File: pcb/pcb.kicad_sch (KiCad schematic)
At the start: 4 parts, among them U1 ESP32-WROOM-32, U2 SCD41-D-R2, U3 BME680, U4 HD44780_I2C

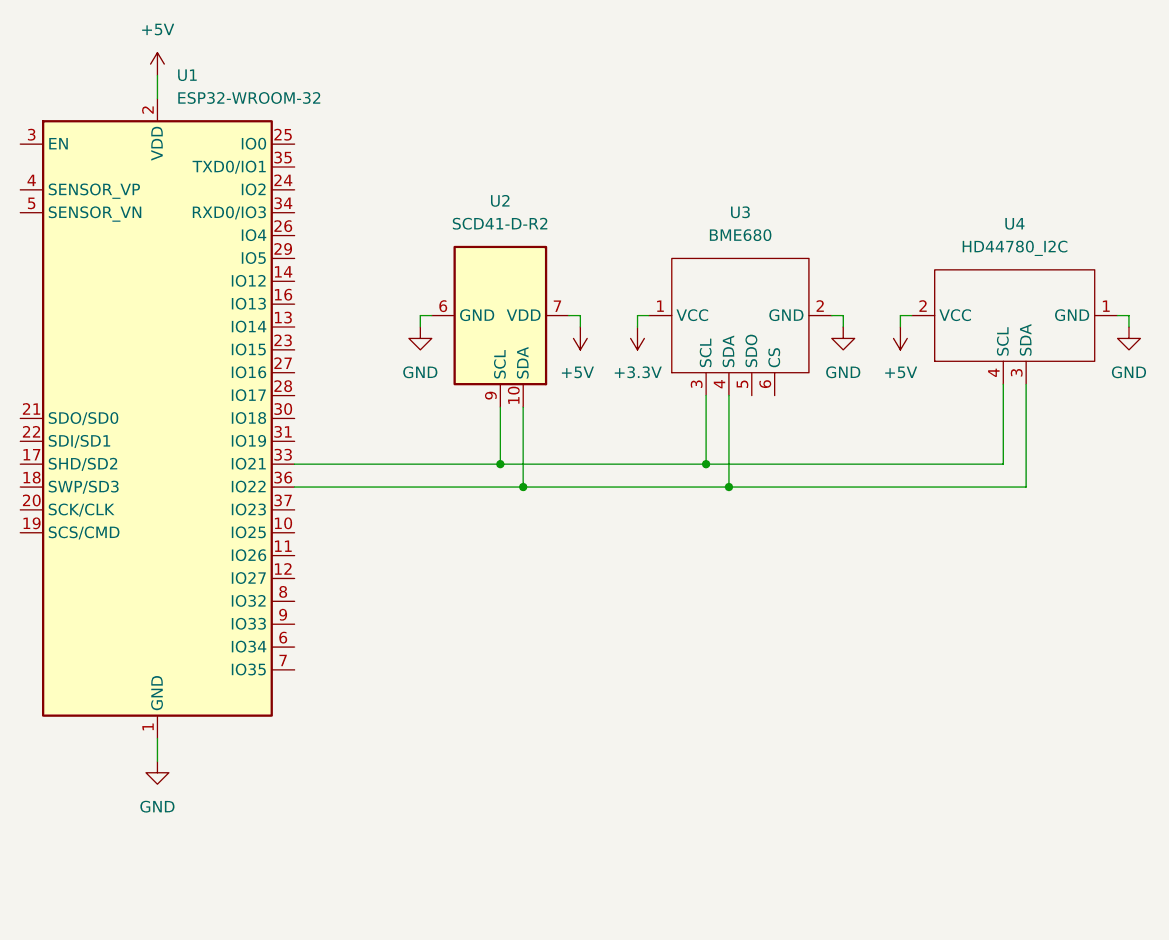
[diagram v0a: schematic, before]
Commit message: add pullup resistors to design
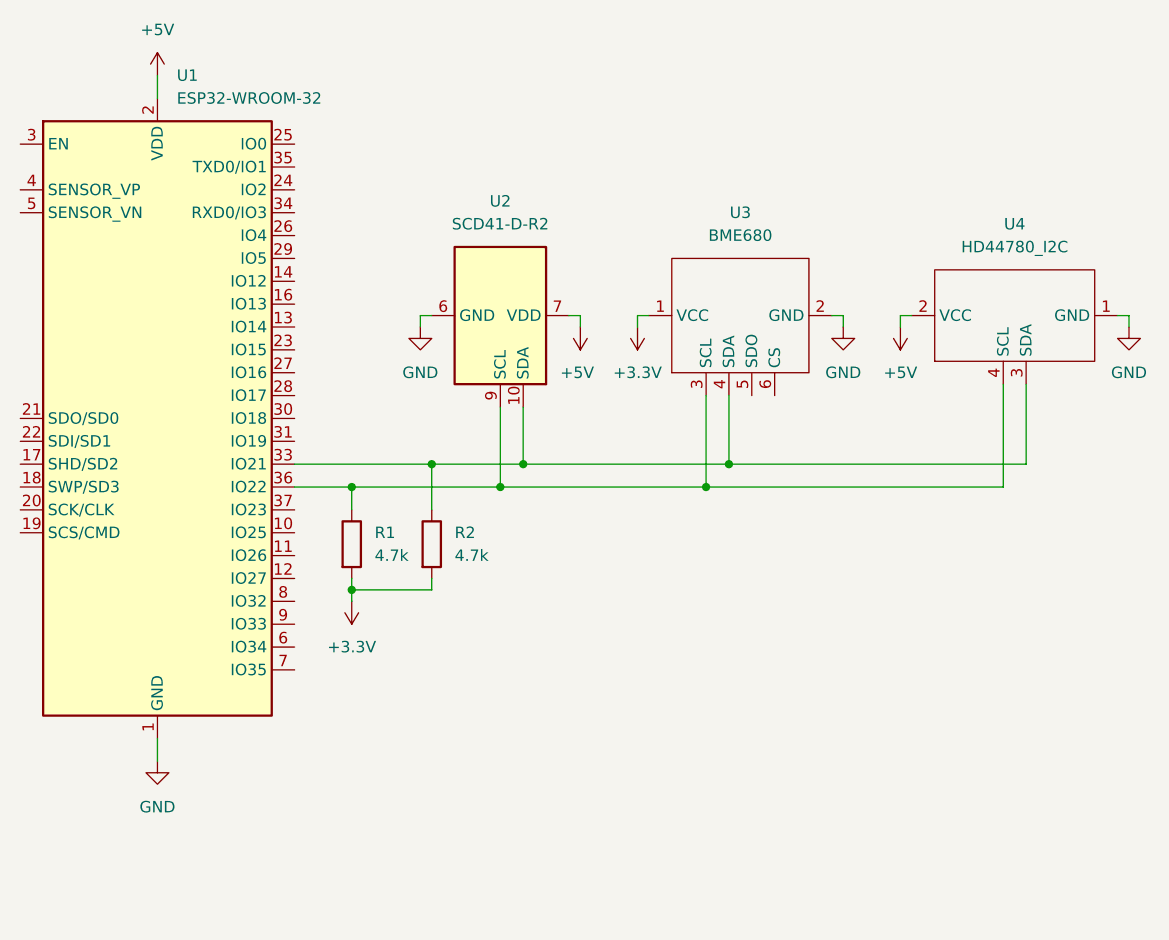
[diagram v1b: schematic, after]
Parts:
- added R1, R2: 4.7k, symbol Device:R
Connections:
- net +3.3V: now also R1.2, R2.2
- net at U2.9 (SCL), U3.3 (SCL), U4.4 (SCL): now also U1.36 (IO22), R1.1; no longer U1.33 (IO21)
- net at U2.10 (SDA), U3.4 (SDA), U4.3 (SDA): now also U1.33 (IO21), R2.1; no longer U1.36 (IO22)

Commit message: update pcb design to split 5v and 3.3v i2c devices
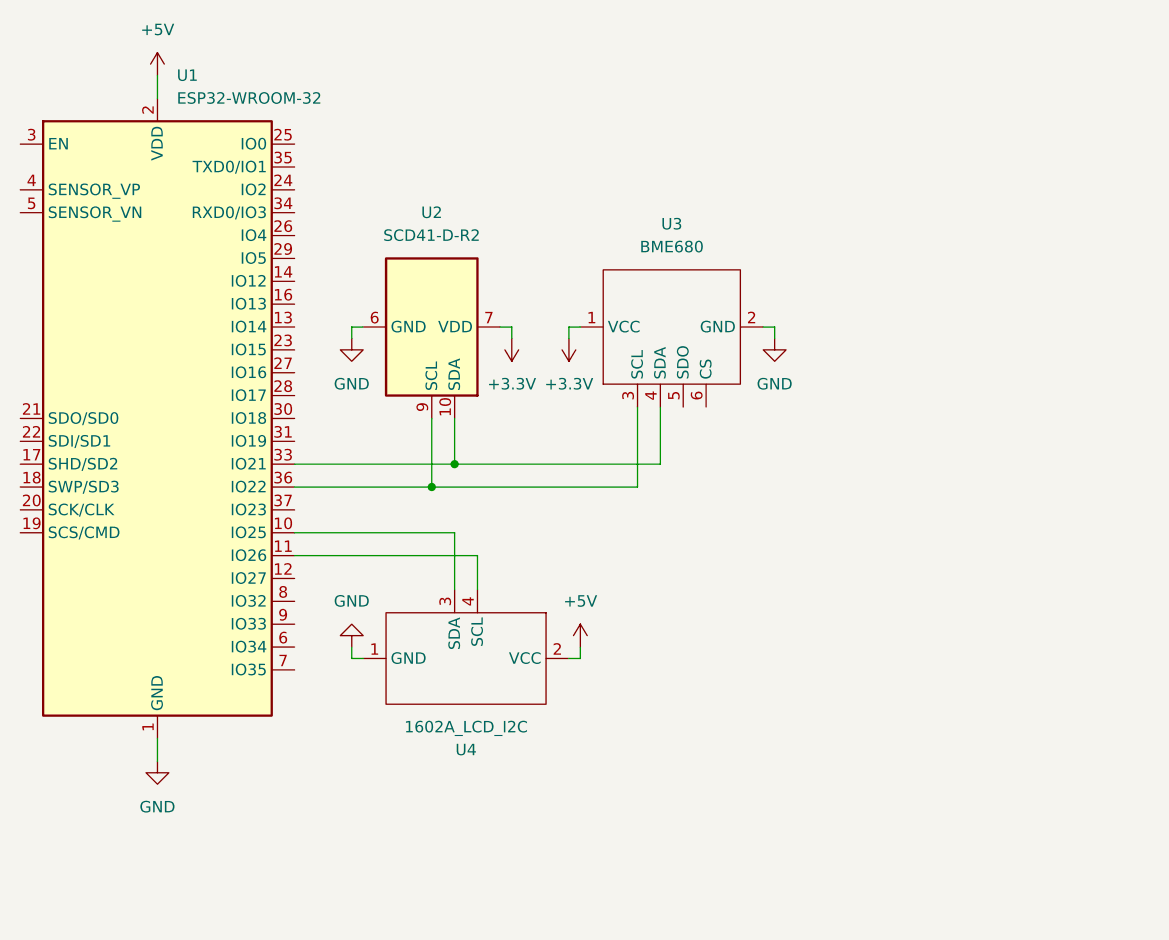
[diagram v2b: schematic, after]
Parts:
- removed R1, R2: 4.7k, symbol Device:R
- U4: value HD44780_I2C -> 1602A_LCD_I2C
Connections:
- net +3.3V: now also U2.19 (VDD), U2.7 (VDD)
- net +5V: no longer U2.19 (VDD), U2.7 (VDD)
- net at U1.33 (IO21), U2.10 (SDA), U3.4 (SDA): no longer U4.3 (SDA)
- net at U1.10 (IO25): now also U4.3 (SDA)
- net at U1.11 (IO26): now also U4.4 (SCL)
- net at U1.36 (IO22), U2.9 (SCL), U3.3 (SCL): no longer U4.4 (SCL)
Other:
- moved on the sheet: U2, U3, U4

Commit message: read sensor data
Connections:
- net GND: now also U3.5 (SDO)
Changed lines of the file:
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@@
+	(wire
+		(pts
+			(xy 170.18 97.79) (xy 170.18 100.33)
+		)
+		(stroke
+			(width 0)
+			(type default)
+		)
+	)
 	(wire
 		(pts
@@
 					(unit 1)
 				)
+			)
+		)
+	)
+	(symbol
+		(lib_id "power:GND")
+		(at 170.18 100.33 0)
+		(unit 1)
+		(exclude_from_sim no)
+		(in_bom yes)
+		(on_board yes)
+		(dnp no)
+		(fields_autoplaced yes)
+		(property "Reference" "#PWR09"
+			(at 170.18 106.68 0)
+			(effects
+				(font
+					(size 1.27 1.27)
+				)
+				(hide yes)
+			)
+		)
+		(property "Value" "GND"
+			(at 170.18 105.41 0)
+			(effects
+				(font
+					(size 1.27 1.27)
+				)
+			)
+		)
+		(property "Footprint" ""
+			(at 170.18 100.33 0)
+			(effects
+				(font
+					(size 1.27 1.27)
+				)
+				(hide yes)
+			)
+		)
+		(property "Datasheet" ""
+			(at 170.18 100.33 0)
+			(effects
+				(font
+					(size 1.27 1.27)
+				)
+				(hide yes)
+			)
+		)
+		(property "Description" "Power symbol creates a global label with name \"GND\" , ground"
+			(at 170.18 100.33 0)
+			(effects
+				(font
+					(size 1.27 1.27)
+				)
+				(hide yes)
+			)
+		)
+		(pin "1"
+		)
+		(instances
+			(project ""
+				(path "/f8392987-3ddd-437f-94e8-8fae610849f1"
+					(reference "#PWR09")
+					(unit 1)
+				)

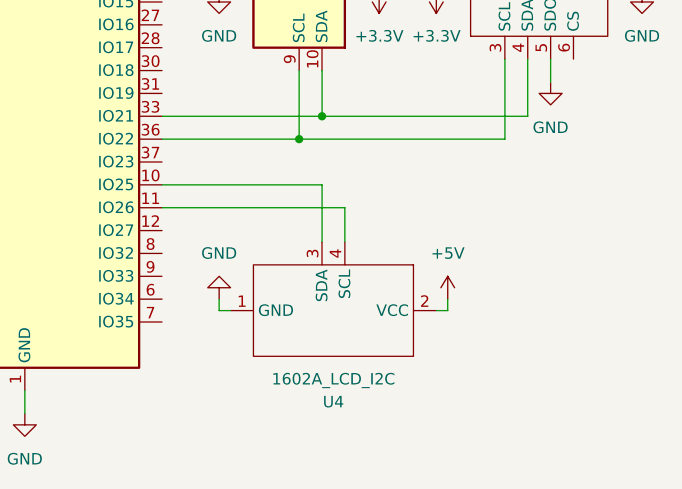
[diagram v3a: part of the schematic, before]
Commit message: add button for selecting displayMode
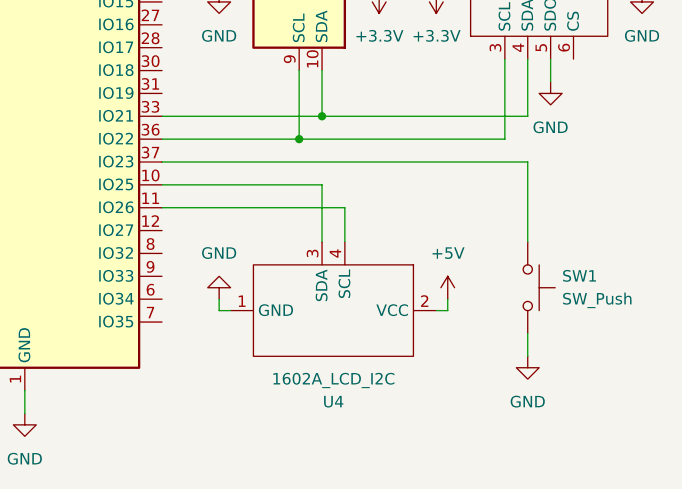
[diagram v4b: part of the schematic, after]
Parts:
- added SW1: SW_Push, symbol Switch:SW_Push
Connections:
- net GND: now also SW1.2
- net at U1.37 (IO23): now also SW1.1
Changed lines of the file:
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@@
+	(wire
+		(pts
+			(xy 167.64 118.11) (xy 167.64 109.22)
+		)
+		(stroke
+			(width 0)
+			(type default)
+		)
+	)
 	(wire
 		(pts
@@
 	(wire
 		(pts
+			(xy 167.64 128.27) (xy 167.64 130.81)
+		)
+		(stroke
+			(width 0)
+			(type default)
+		)
+	)
+	(wire
+		(pts
 			(xy 157.48 88.9) (xy 158.75 88.9)
 		)
@@
 		(pts
 			(xy 144.78 111.76) (xy 144.78 118.11)
+		)
+		(stroke
+			(width 0)
+			(type default)
+		)
+	)
+	(wire
+		(pts
+			(xy 167.64 109.22) (xy 127 109.22)
 		)
 		(stroke
@@
 	)
 	(symbol
+		(lib_id "power:GND")
+		(at 167.64 130.81 0)
+		(unit 1)
+		(exclude_from_sim no)
+		(in_bom yes)
+		(on_board yes)
+		(dnp no)
+		(fields_autoplaced yes)
+		(property "Reference" "#PWR010"
+			(at 167.64 137.16 0)
+			(effects
+				(font
+					(size 1.27 1.27)
+				)
+				(hide yes)
+			)
+		)
+		(property "Value" "GND"
+			(at 167.64 135.89 0)
+			(effects
+				(font
+					(size 1.27 1.27)
+				)
+			)
+		)
+		(property "Footprint" ""
+			(at 167.64 130.81 0)
+			(effects
+				(font
+					(size 1.27 1.27)
+				)
+				(hide yes)
+			)
+		)
+		(property "Datasheet" ""
+			(at 167.64 130.81 0)
+			(effects
+				(font
+					(size 1.27 1.27)
+				)
+				(hide yes)
+			)
+		)
+		(property "Description" "Power symbol creates a global label with name \"GND\" , ground"
+			(at 167.64 130.81 0)
+			(effects
+				(font
+					(size 1.27 1.27)
+				)
+				(hide yes)
+			)
+		)
+		(pin "1"
+		)
+		(instances
+			(project ""
+				(path "/f8392987-3ddd-437f-94e8-8fae610849f1"
+					(reference "#PWR010")
+					(unit 1)
+				)
+			)
+		)
+	)
+	(symbol
 		(lib_id "power:+3.3V")
 		(at 157.48 90.17 180)
@@
 					(unit 1)
 				)
+			)
+		)
+	)
+	(symbol
+		(lib_id "Switch:SW_Push")
+		(at 167.64 123.19 270)
+		(unit 1)
+		(exclude_from_sim no)
+		(in_bom yes)
+		(on_board yes)
+		(dnp no)
+		(fields_autoplaced yes)
+		(property "Reference" "SW1"
+			(at 171.45 121.9199 90)
+			(effects
+				(font
+					(size 1.27 1.27)
+				)
+				(justify left)
+			)
+		)
+		(property "Value" "SW_Push"
+			(at 171.45 124.4599 90)
+			(effects
+				(font
+					(size 1.27 1.27)
+				)
+				(justify left)
+			)
+		)
+		(property "Footprint" ""
+			(at 172.72 123.19 0)
+			(effects
+				(font
+					(size 1.27 1.27)
+				)
+				(hide yes)
+			)
+		)
+		(property "Datasheet" "~"
+			(at 172.72 123.19 0)
+			(effects
+				(font
+					(size 1.27 1.27)
+				)
+				(hide yes)
+			)
+		)
+		(property "Description" "Push button switch, generic, two pins"
+			(at 167.64 123.19 0)
+			(effects
+				(font
+					(size 1.27 1.27)
+				)
+				(hide yes)
+			)
+		)
+		(pin "2"
+		)
+		(pin "1"
+		)
+		(instances
+			(project ""
+				(path "/f8392987-3ddd-437f-94e8-8fae610849f1"
+					(reference "SW1")
+					(unit 1)
+				)

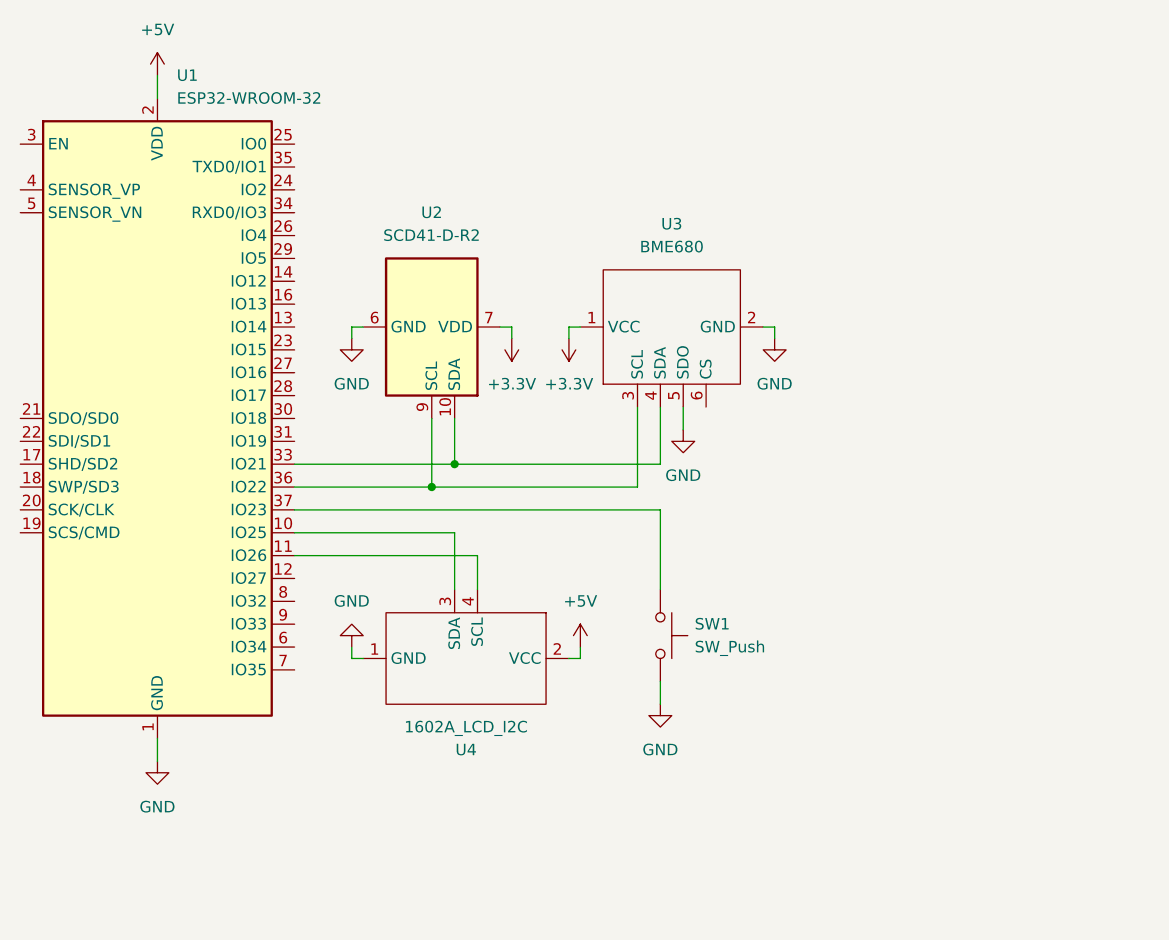
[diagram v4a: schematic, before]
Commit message: add brighness reader
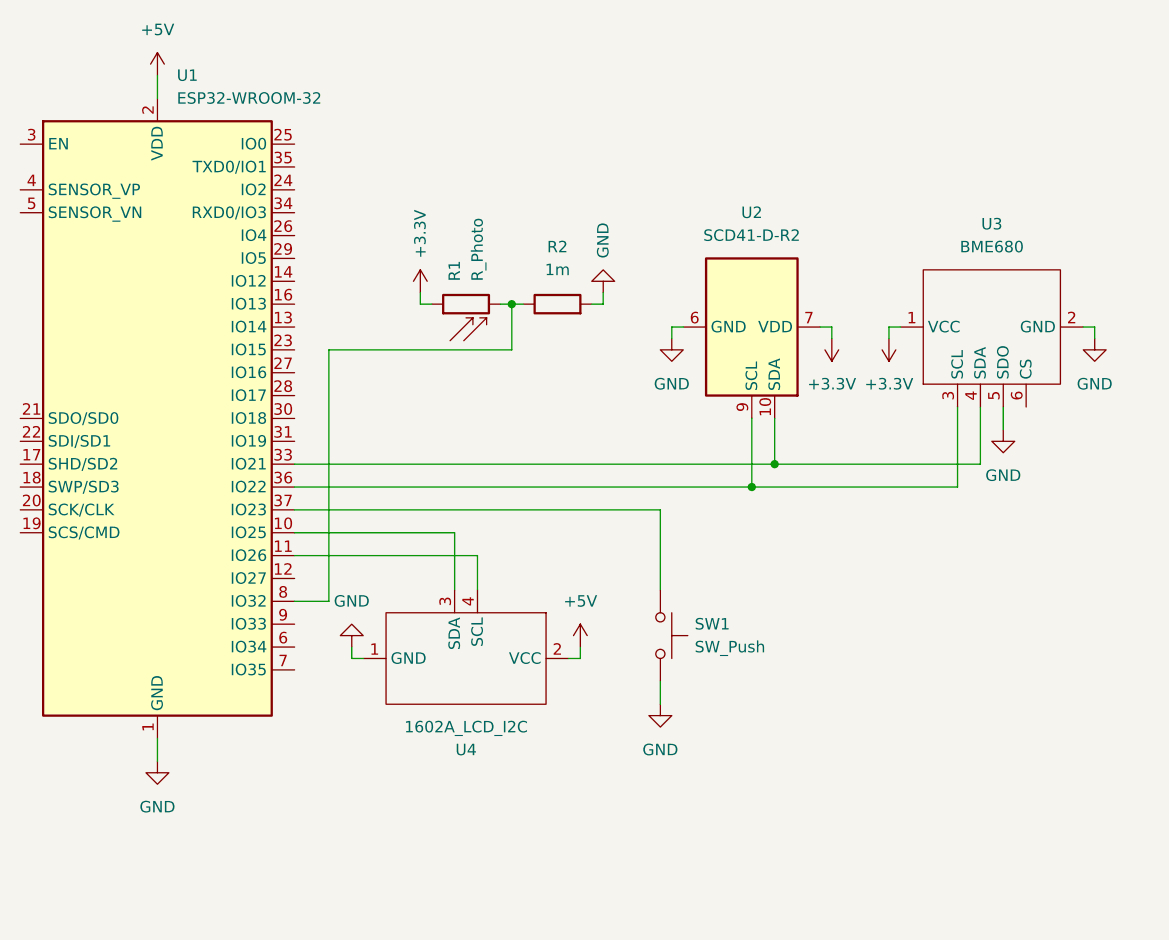
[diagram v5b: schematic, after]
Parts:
- added R1: R_Photo, symbol Device:R_Photo
- added R2: 1m, symbol Device:R
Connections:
- net +3.3V: now also R1.1
- net GND: now also R2.2
- net at U1.8 (IO32): now also R1.2, R2.1
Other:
- moved on the sheet: U2, U3

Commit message: basic setup pwm for backlight
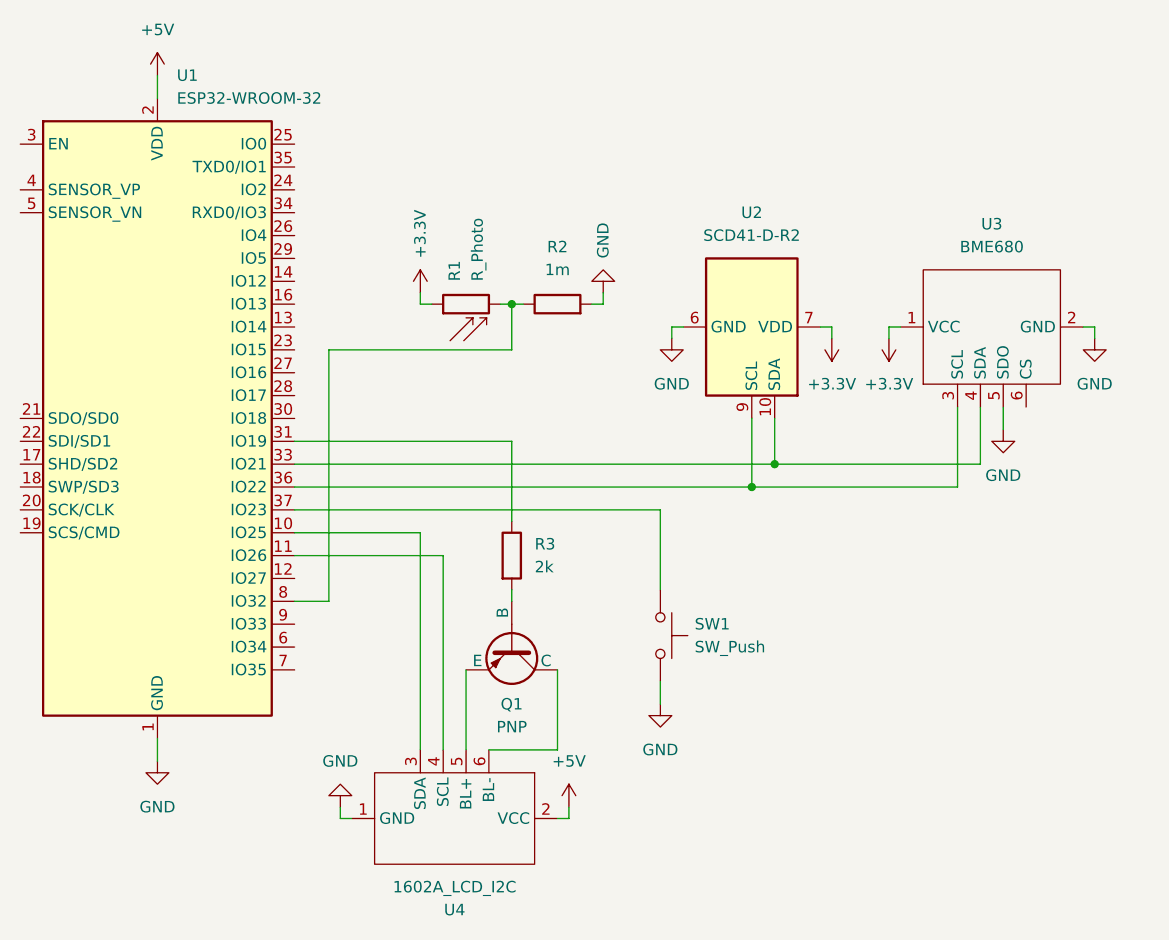
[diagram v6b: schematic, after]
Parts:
- added Q1: PNP, symbol Simulation_SPICE:PNP
- added R3: 2k, symbol Device:R
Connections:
- net at U1.31 (IO19): now also R3.1
- new net: Q1.3 (E), U4.5 (BL+)
- new net: Q1.1 (C), U4.6 (BL-)
- new net: Q1.2 (B), R3.2
